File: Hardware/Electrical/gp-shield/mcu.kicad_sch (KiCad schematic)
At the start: 87 parts, among them J3 Conn_01x04, Q3 Q_NMOS_GDS, SW2 SW_Push, SW3 SW_Push

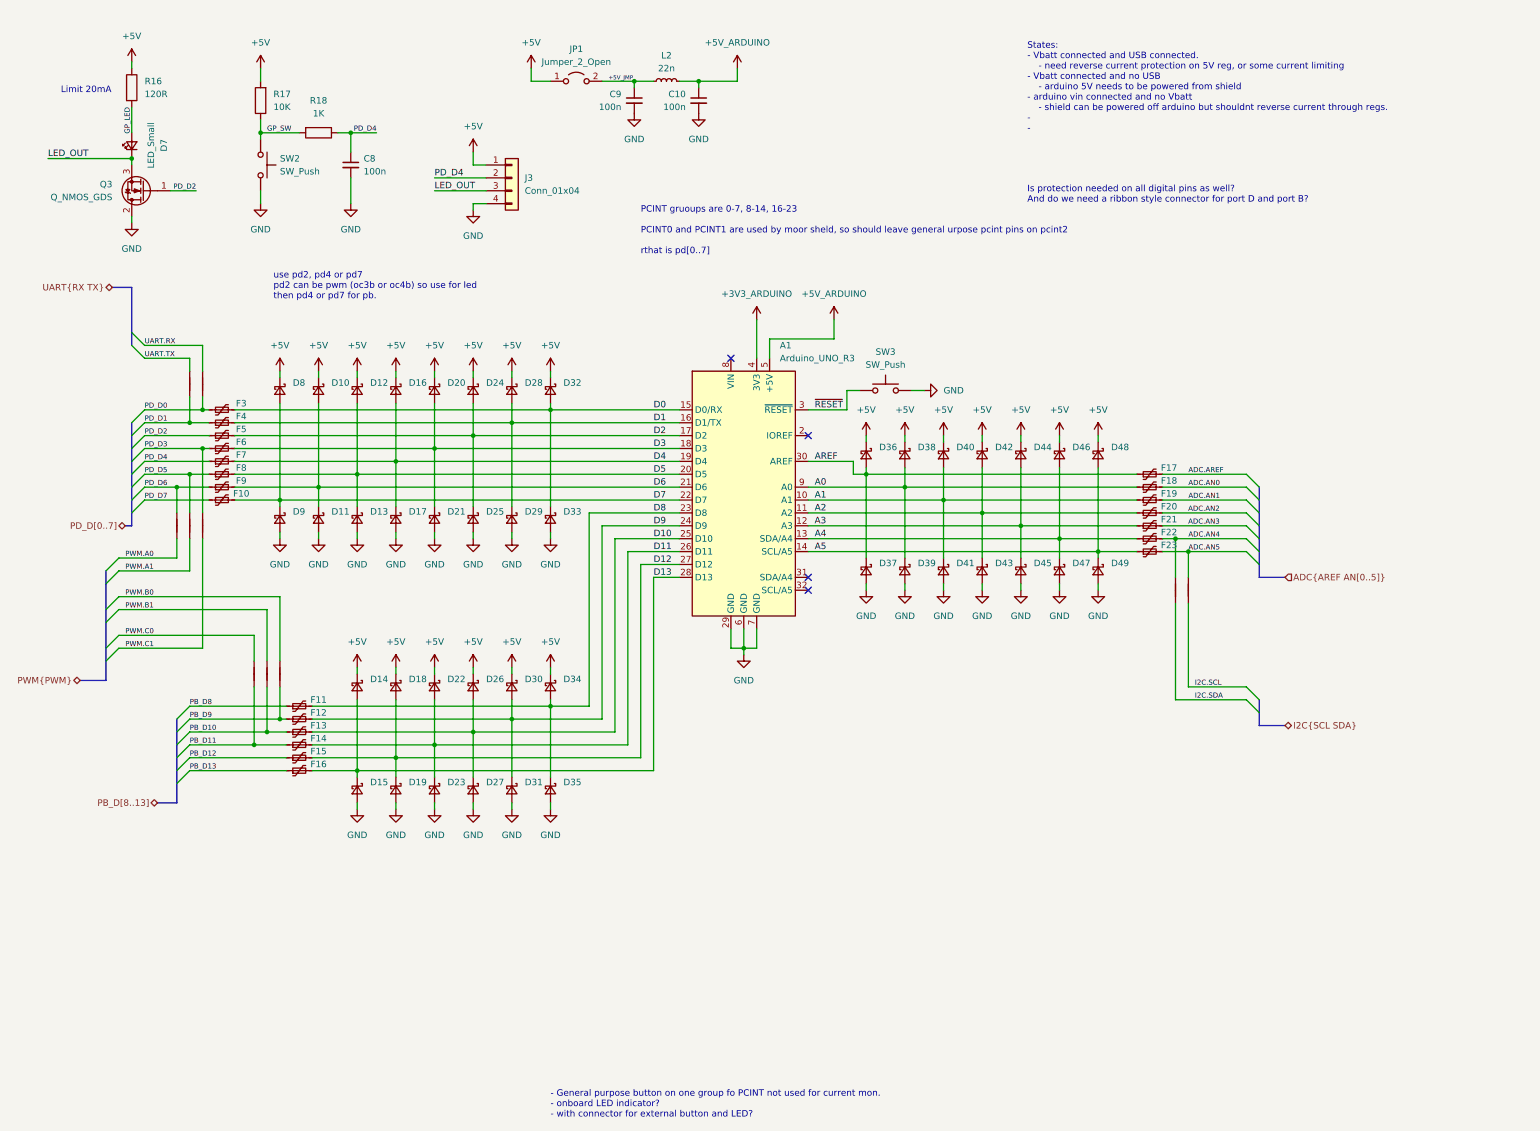
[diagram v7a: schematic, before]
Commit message: Complete draft PCB layout
Added updated renders to doc.
Added some documentation to schematic
complete PCB layout with some revisions still needed
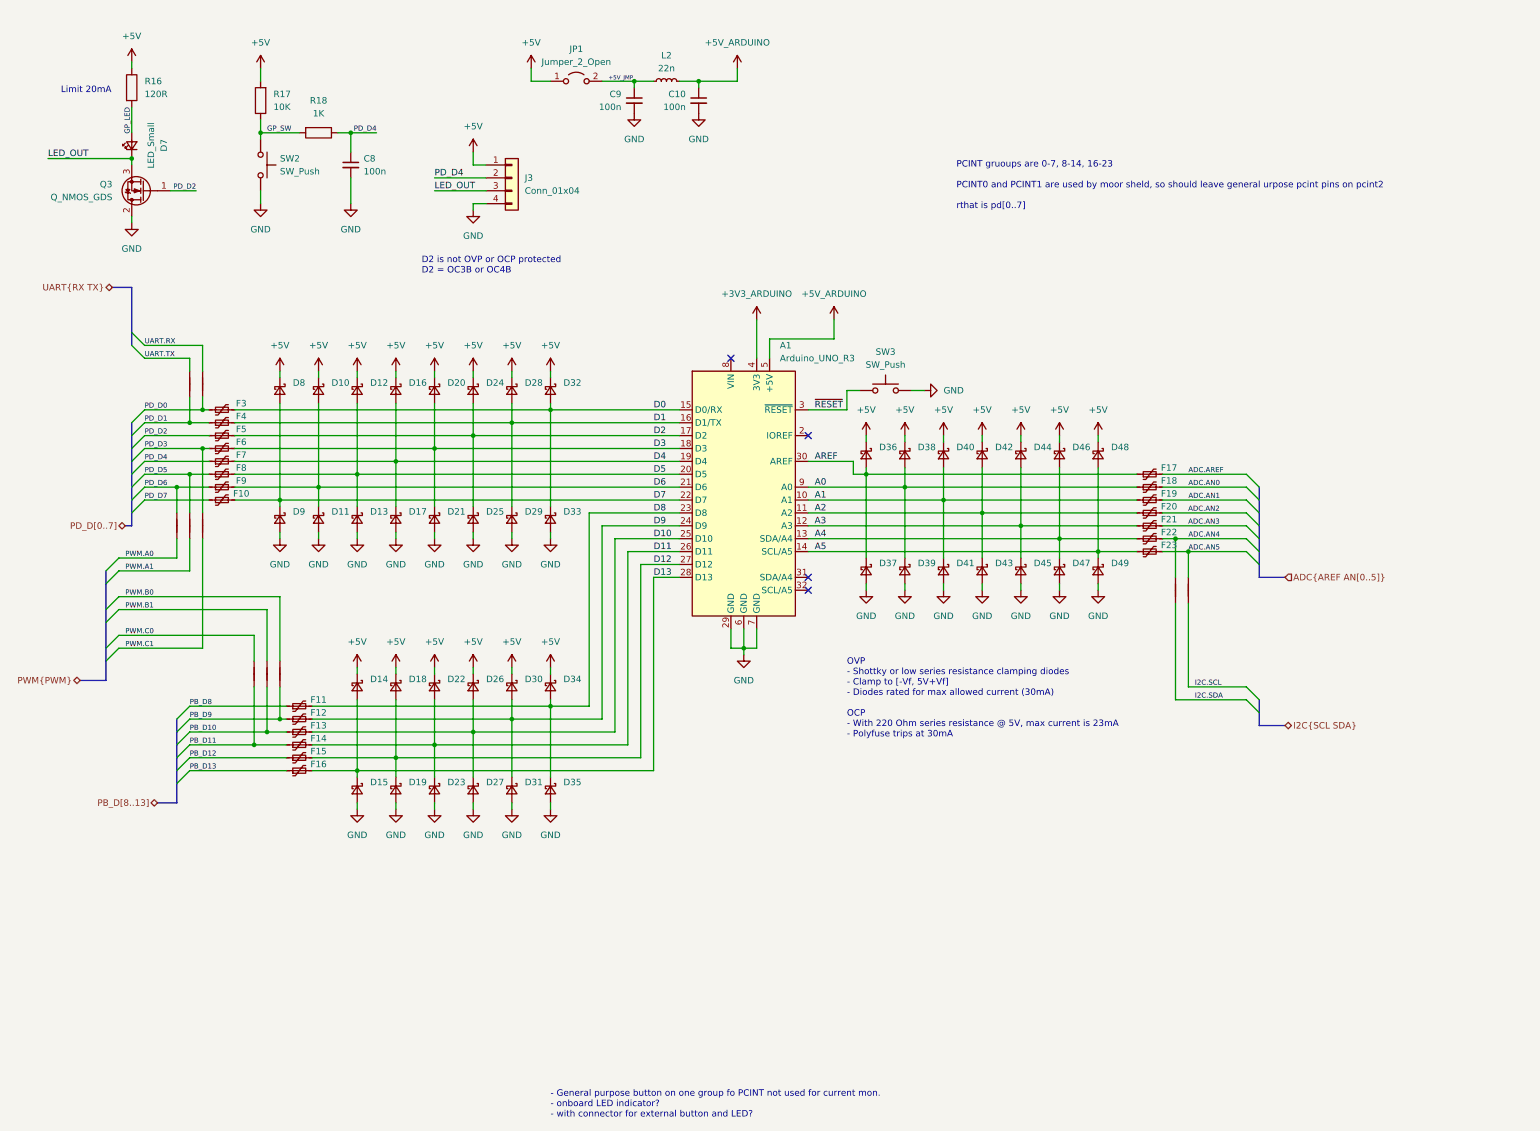
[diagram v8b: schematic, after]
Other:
- note added: "D2 is not OVP or OCP protected D2 = OC3B or OC4B"
- note added: "OVP - Shottky or low series resistance clamping diodes - Clamp to [-Vf, 5V+Vf] - Diodes rated for max allowed current (30mA) OCP - With 220 Ohm series resistance @ 5V, max current is 23mA - Polyfuse trips at 30mA"
- note removed: "Is protection needed on all digital pins as well? And do we need a ribbon style connector for port D and port B?"
- note removed: "States: - Vbatt connected and USB connected. - need reverse current protection on 5V reg, or some current limiting - Vbatt connected and no USB - arduino 5V needs to be powered from shield - arduino vin connected and no Vbatt - shield can be powered off arduino but shouldnt reverse current through regs. - -"
- note removed: "use pd2, pd4 or pd7 pd2 can be pwm (oc3b or oc4b) so use for led then pd4 or pd7 for pb."
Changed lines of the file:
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@@
     (stroke (width 0) (type default) (color 0 0 0 0))
   )
-  (text "use pd2, pd4 or pd7\npd2 can be pwm (oc3b or oc4b) so use for led\nthen pd4 or pd7 for pb.\n"
-    (at 63.5 67.31 0)
+  (text "D2 is not OVP or OCP protected\nD2 = OC3B or OC4B\n" (at 92.71 62.23 0)
+    (effects (font (size 1.27 1.27)) (justify left bottom))
+  )
+  (text "OVP\n- Shottky or low series resistance clamping diodes\n- Clamp to [-Vf, 5V+Vf]\n- Diodes rated for max allowed current (30mA)\n\nOCP\n- With 220 Ohm series resistance @ 5V, max current is 23mA\n- Polyfuse trips at 30mA"
+    (at 176.53 153.67 0)
     (effects (font (size 1.27 1.27)) (justify left bottom))
   )
   (text "PCINT gruoups are 0-7, 8-14, 16-23\n\nPCINT0 and PCINT1 are used by moor sheld, so should leave general urpose pcint pins on pcint2\n\nrthat is pd[0..7]"
-    (at 135.89 58.42 0)
-    (effects (font (size 1.27 1.27)) (justify left bottom))
-  )
-  (text "States:\n- Vbatt connected and USB connected.\n	- need reverse current protection on 5V reg, or some current limiting\n- Vbatt connected and no USB\n	- arduino 5V needs to be powered from shield\n- arduino vin connected and no Vbatt\n	- shield can be powered off arduino but shouldnt reverse current through regs.\n- \n- "
-    (at 212.09 34.29 0)
+    (at 198.12 49.53 0)
     (effects (font (size 1.27 1.27)) (justify left bottom))
   )
@@
     (effects (font (size 1.27 1.27)) (justify left bottom))
   )
-  (text "Is protection needed on all digital pins as well?\nAnd do we need a ribbon style connector for port D and port B?"
-    (at 212.09 48.26 0)
-    (effects (font (size 1.27 1.27)) (justify left bottom))
-  )
